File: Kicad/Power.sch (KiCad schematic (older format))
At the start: 1 part

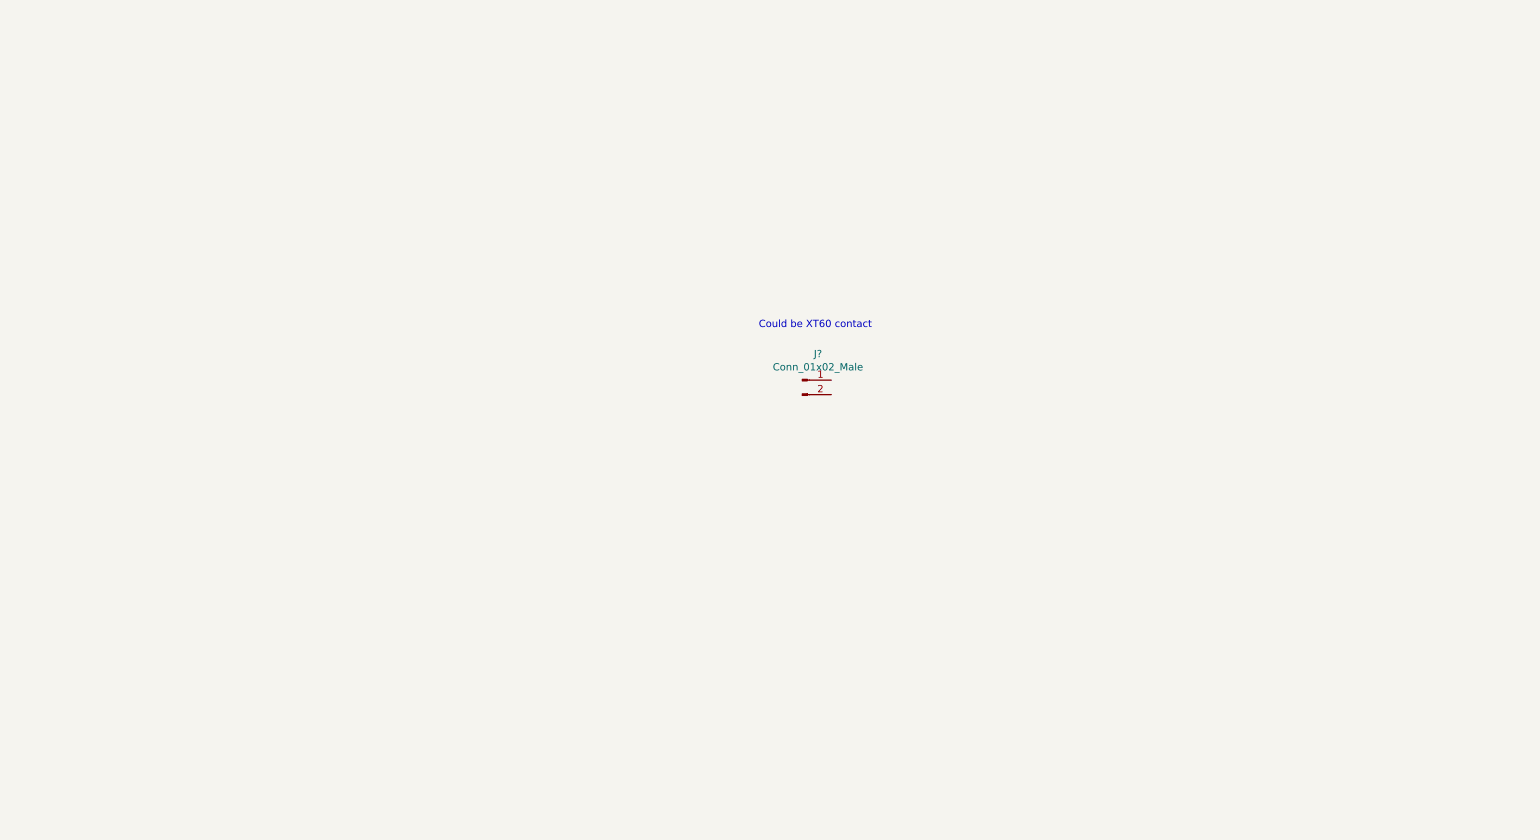
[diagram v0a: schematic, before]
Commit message: Added stepper driver and componets and power management
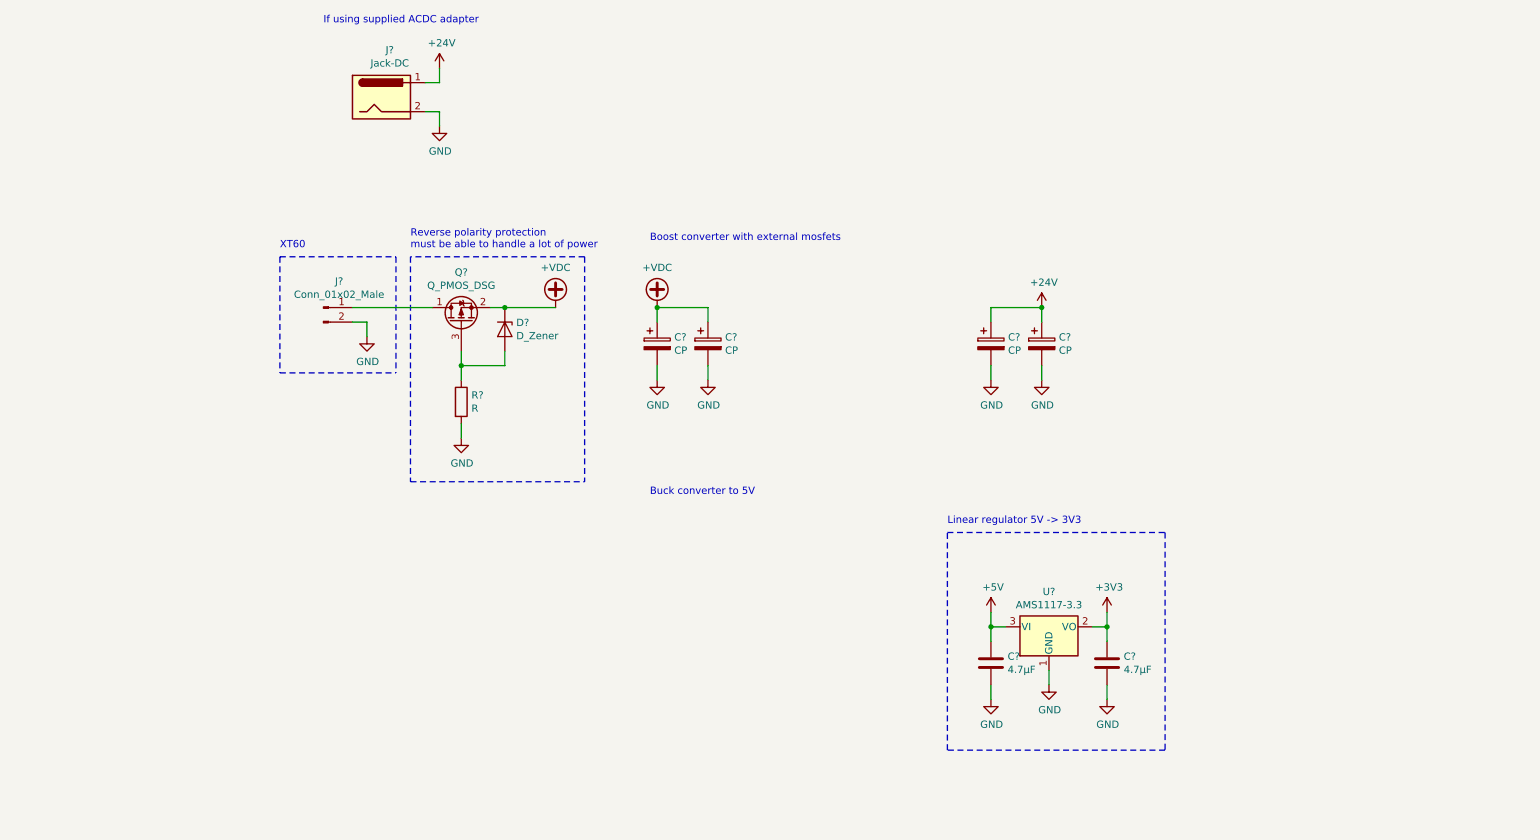
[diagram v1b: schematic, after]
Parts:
- added C? (x4): CP, symbol Device:CP
- added C? (x2): 4.7µF, symbol Device:C
- added D?: D_Zener, symbol Device:D_Zener
- added J?: Jack-DC, symbol Connector:Jack-DC
- added Q?: Q_PMOS_DSG, symbol Device:Q_PMOS_DSG
- added R?: R, symbol Device:R
- added U?: AMS1117-3.3, Package_TO_SOT_SMD:SOT-223-3_TabPin2, symbol Regulator_Linear:AMS1117-3.3
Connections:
- net at J?.1 (Pin_1): now also Q?.1 (D)
- net GND: now reaches J?.2 (Pin_2)
- net GND: now also C?.2, C?.2, C?.2, C?.2, C?.2, C?.2, J?.2, R?.2, U?.1 (GND)
- new net: D?.2 (A), Q?.3 (G), R?.1
- new net +24V: C?.1, C?.1, J?.1
- new net +3V3: C?.1, U?.2 (VO)
- new net +5V: C?.1, U?.3 (VI)
- new net +VDC: C?.1, C?.1, D?.1 (K), Q?.2 (S)
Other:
- note added: "Boost converter with external mosfets"
- note added: "Buck converter to 5V"
- note added: "If using supplied ACDC adapter"
- note added: "Linear regulator 5V -> 3V3"
- note added: "Reverse polarity protection\nmust be able to handle a lot of power"
- note added: "XT60"
- note removed: "Could be XT60 contact"
- moved on the sheet: J?

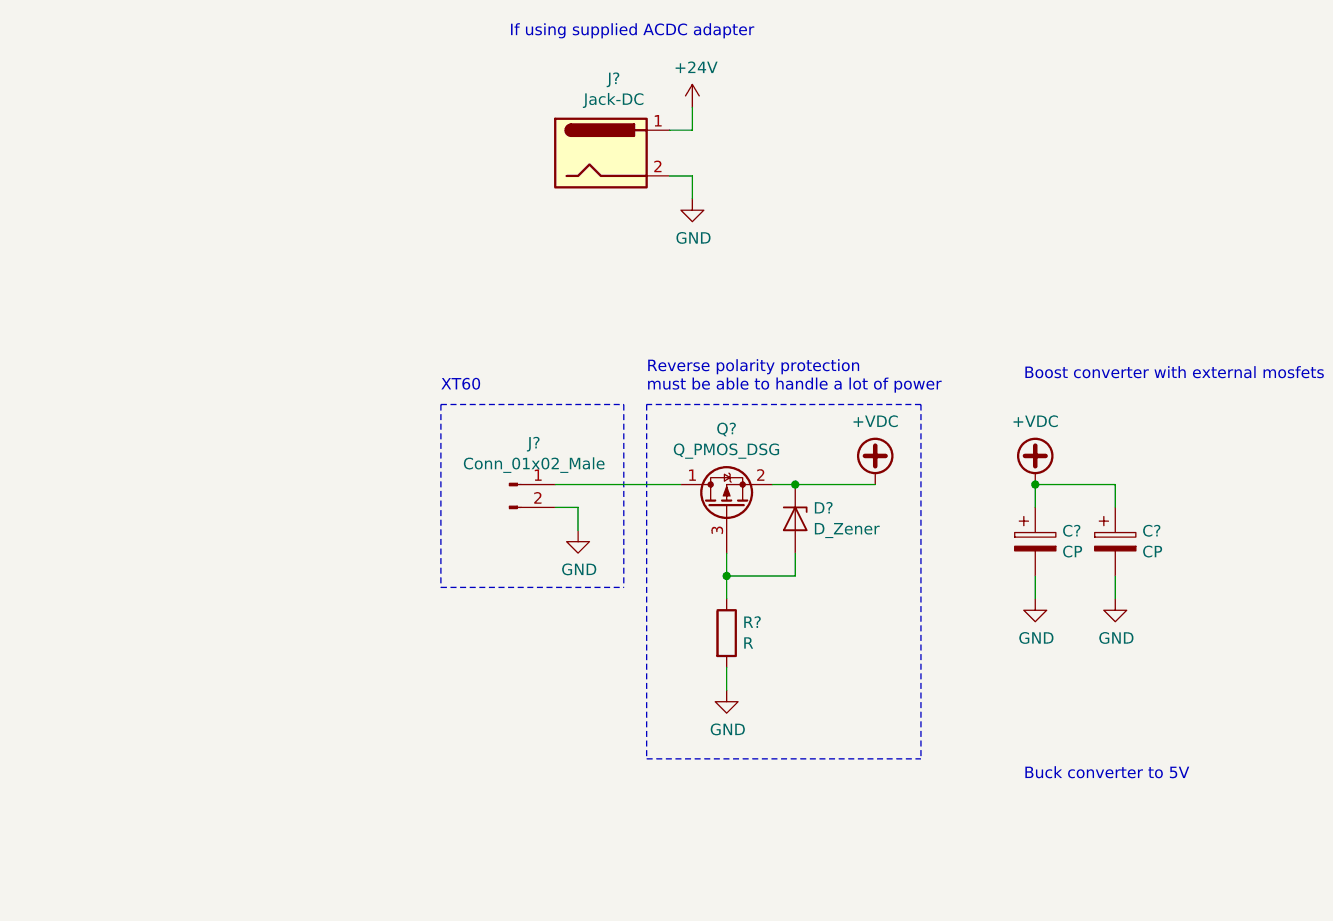
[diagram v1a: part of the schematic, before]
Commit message: Added spindle sheet
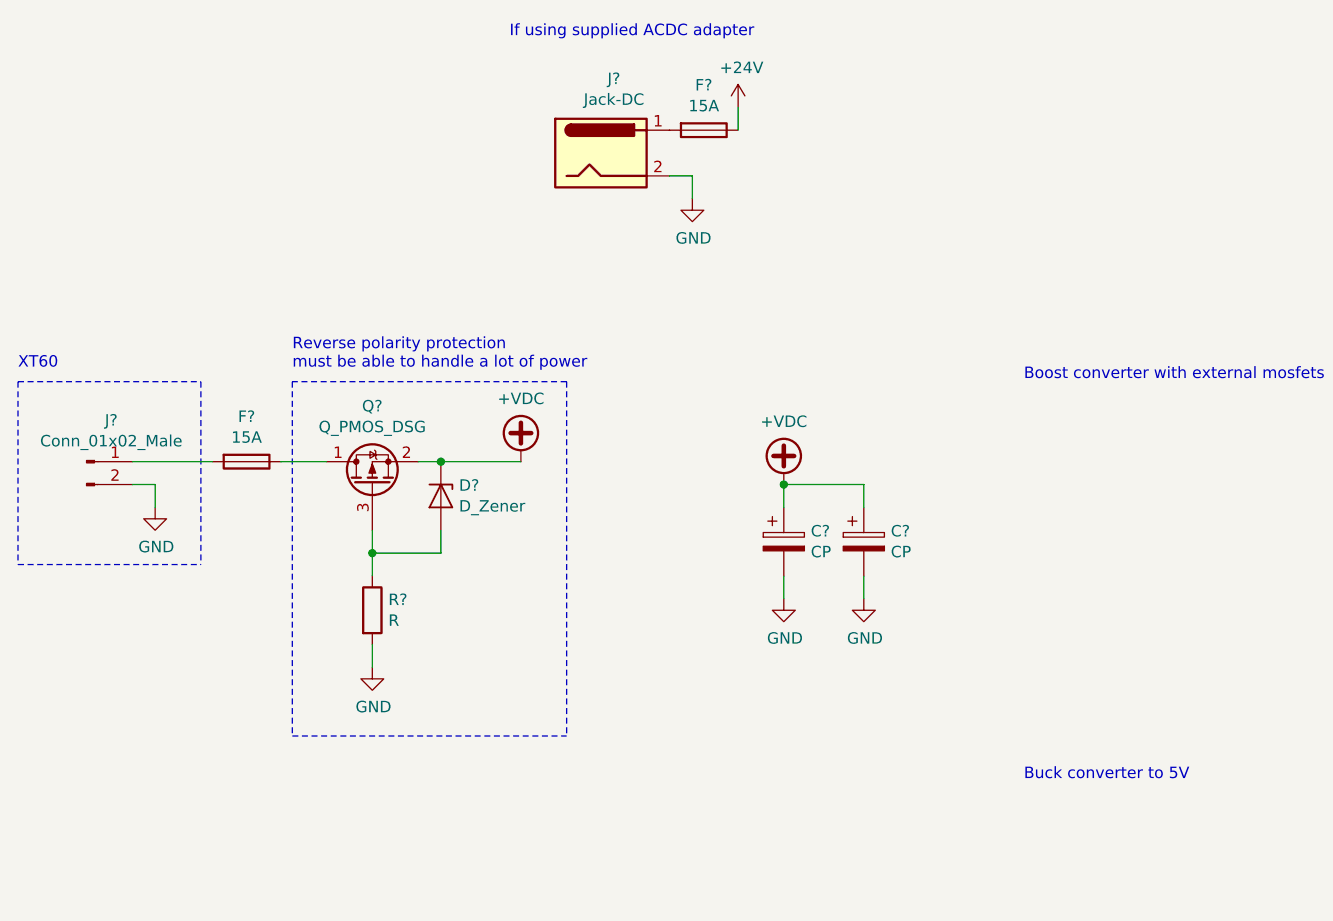
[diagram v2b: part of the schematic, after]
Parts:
- added F? (x2): 15A, symbol Device:Fuse
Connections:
- net +24V: now also F?.1; no longer J?.1
- net at J?.1 (Pin_1): now also F?.2; no longer Q?.1 (D)
- new net: F?.2, J?.1
- new net: F?.1, Q?.1 (D)
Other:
- moved on the sheet: C?, D?, J?, Q?, R?
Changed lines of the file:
@@
 $Descr A4 11693 8268
 encoding utf-8
-Sheet 3 4
+Sheet 3 5
 Title ""
 Date ""
@@
 L Connector:Conn_01x02_Male J?
 U 1 1 5E1C9929
-P 2700 3450
-F 0 "J?" H 2808 3631 50  0000 C CNN
-F 1 "Conn_01x02_Male" H 2808 3540 50  0000 C CNN
-F 2 "" H 2700 3450 50  0001 C CNN
-F 3 "~" H 2700 3450 50  0001 C CNN
-	1    2700 3450
-	1    0    0    -1
-$EndComp
-Text Notes 2400 3050 0    50   ~ 0
+P 850 3350
+F 0 "J?" H 958 3531 50  0000 C CNN
+F 1 "Conn_01x02_Male" H 958 3440 50  0000 C CNN
+F 2 "" H 850 3350 50  0001 C CNN
+F 3 "~" H 850 3350 50  0001 C CNN
+	1    850  3350
+	1    0    0    -1
+$EndComp
+Text Notes 550  2950 0    50   ~ 0
 XT60
 Text Notes 4950 3000 0    50   ~ 0
@@
 L power:+VDC #PWR0110
 U 1 1 5E1F3FCE
-P 4300 3450
-F 0 "#PWR0110" H 4300 3350 50  0001 C CNN
-F 1 "+VDC" H 4300 3725 50  0000 C CNN
-F 2 "" H 4300 3450 50  0001 C CNN
-F 3 "" H 4300 3450 50  0001 C CNN
-	1    4300 3450
+P 2750 3350
+F 0 "#PWR0110" H 2750 3250 50  0001 C CNN
+F 1 "+VDC" H 2750 3625 50  0000 C CNN
+F 2 "" H 2750 3350 50  0001 C CNN
+F 3 "" H 2750 3350 50  0001 C CNN
+	1    2750 3350
 	1    0    0    -1
 $EndComp
@@
 L power:GND #PWR0111
 U 1 1 5E1F4248
-P 3000 3650
-F 0 "#PWR0111" H 3000 3400 50  0001 C CNN
-F 1 "GND" H 3005 3477 50  0000 C CNN
-F 2 "" H 3000 3650 50  0001 C CNN
-F 3 "" H 3000 3650 50  0001 C CNN
-	1    3000 3650
+P 1150 3550
+F 0 "#PWR0111" H 1150 3300 50  0001 C CNN
+F 1 "GND" H 1155 3377 50  0000 C CNN
+F 2 "" H 1150 3550 50  0001 C CNN
+F 3 "" H 1150 3550 50  0001 C CNN
+	1    1150 3550
 	1    0    0    -1
 $EndComp
@@
 L power:+24V #PWR0113
 U 1 1 5E1F962C
-P 3500 1800
-F 0 "#PWR0113" H 3500 1650 50  0001 C CNN
-F 1 "+24V" H 3515 1973 50  0000 C CNN
-F 2 "" H 3500 1800 50  0001 C CNN
-F 3 "" H 3500 1800 50  0001 C CNN
-	1    3500 1800
-	1    0    0    -1
-$EndComp
-Wire Wire Line
-	3500 1800 3500 1900
-Wire Wire Line
-	3500 1900 3400 1900
+P 3700 1800
+F 0 "#PWR0113" H 3700 1650 50  0001 C CNN
+F 1 "+24V" H 3715 1973 50  0000 C CNN
+F 2 "" H 3700 1800 50  0001 C CNN
+F 3 "" H 3700 1800 50  0001 C CNN
+	1    3700 1800
+	1    0    0    -1
+$EndComp
 Wire Wire Line
 	3400 2100 3500 2100
@@
 L Device:Q_PMOS_DSG Q?
 U 1 1 5E1FCACA
-P 3650 3550
-F 0 "Q?" V 3993 3550 50  0000 C CNN
-F 1 "Q_PMOS_DSG" V 3902 3550 50  0000 C CNN
-F 2 "" H 3850 3650 50  0001 C CNN
-F 3 "~" H 3650 3550 50  0001 C CNN
-	1    3650 3550
+P 2100 3450
+F 0 "Q?" V 2443 3450 50  0000 C CNN
+F 1 "Q_PMOS_DSG" V 2352 3450 50  0000 C CNN
+F 2 "" H 2300 3550 50  0001 C CNN
+F 3 "~" H 2100 3450 50  0001 C CNN
+	1    2100 3450
 	0    -1   -1   0
 $EndComp
@@
 L power:GND #PWR0114
 U 1 1 5E20125D
-P 3650 4350
-F 0 "#PWR0114" H 3650 4100 50  0001 C CNN
-F 1 "GND" H 3655 4177 50  0000 C CNN
-F 2 "" H 3650 4350 50  0001 C CNN
-F 3 "" H 3650 4350 50  0001 C CNN
-	1    3650 4350
-	1    0    0    -1
-$EndComp
-Wire Wire Line
-	3950 3850 3650 3850
-Wire Wire Line
-	3950 3750 3950 3850
-Wire Wire Line
-	3650 3750 3650 3850
+P 2100 4250
+F 0 "#PWR0114" H 2100 4000 50  0001 C CNN
+F 1 "GND" H 2105 4077 50  0000 C CNN
+F 2 "" H 2100 4250 50  0001 C CNN
+F 3 "" H 2100 4250 50  0001 C CNN
+	1    2100 4250
+	1    0    0    -1
+$EndComp
+Wire Wire Line
+	2400 3750 2100 3750
+Wire Wire Line
+	2400 3650 2400 3750
+Wire Wire Line
+	2100 3650 2100 3750
 $Comp
 L Device:R R?
 U 1 1 5E202E4D
-P 3650 4100
-F 0 "R?" H 3720 4146 50  0000 L CNN
-F 1 "R" H 3720 4055 50  0000 L CNN
-F 2 "" V 3580 4100 50  0001 C CNN
-F 3 "~" H 3650 4100 50  0001 C CNN
-	1    3650 4100
-	1    0    0    -1
-$EndComp
-Wire Wire Line
-	3650 3850 3650 3950
-Connection ~ 3650 3850
-Wire Wire Line
-	3650 4250 3650 4350
-Wire Wire Line
-	3000 3650 3000 3550
-Wire Wire Line
-	3000 3550 2900 3550
-Wire Notes Line
-	4500 3100 3300 3100
-Wire Notes Line
-	3300 4650 4500 4650
-Text Notes 3300 3050 0    50   ~ 0
+P 2100 4000
+F 0 "R?" H 2170 4046 50  0000 L CNN
+F 1 "R" H 2170 3955 50  0000 L CNN
+F 2 "" V 2030 4000 50  0001 C CNN
+F 3 "~" H 2100 4000 50  0001 C CNN
+	1    2100 4000
+	1    0    0    -1
+$EndComp
+Wire Wire Line
+	2100 3750 2100 3850
+Connection ~ 2100 3750
+Wire Wire Line
+	2100 4150 2100 4250
+Wire Wire Line
+	1150 3550 1150 3450
+Wire Wire Line
+	1150 3450 1050 3450
+Wire Notes Line
+	2950 3000 1750 3000
+Wire Notes Line
+	1750 4550 2950 4550
+Text Notes 1750 2950 0    50   ~ 0
 Reverse polarity protection\nmust be able to handle a lot of power
-Wire Wire Line
-	2900 3450 3450 3450
-Wire Notes Line
-	2400 3100 3200 3100
-Wire Notes Line
-	2400 3900 3200 3900
-Wire Notes Line
-	2400 3100 2400 3900
-Wire Notes Line
-	3200 3100 3200 3900
-Wire Notes Line
-	3300 3100 3300 4650
-Wire Notes Line
-	4500 3100 4500 4650
+Wire Notes Line
+	550  3000 1350 3000
+Wire Notes Line
+	550  3800 1350 3800
+Wire Notes Line
+	550  3000 550  3800
+Wire Notes Line
+	1350 3000 1350 3800
+Wire Notes Line
+	1750 3000 1750 4550
+Wire Notes Line
+	2950 3000 2950 4550
 $Comp
 L Device:CP C?
 U 1 1 5E20A92D
-P 5000 3700
-F 0 "C?" H 5118 3746 50  0000 L CNN
-F 1 "CP" H 5118 3655 50  0000 L CNN
-F 2 "" H 5038 3550 50  0001 C CNN
-F 3 "~" H 5000 3700 50  0001 C CNN
-	1    5000 3700
+P 3900 3700
+F 0 "C?" H 4018 3746 50  0000 L CNN
+F 1 "CP" H 4018 3655 50  0000 L CNN
+F 2 "" H 3938 3550 50  0001 C CNN
+F 3 "~" H 3900 3700 50  0001 C CNN
+	1    3900 3700
 	1    0    0    -1
 $EndComp
@@
 L Device:CP C?
 U 1 1 5E20B915
-P 5350 3700
-F 0 "C?" H 5468 3746 50  0000 L CNN
-F 1 "CP" H 5468 3655 50  0000 L CNN
-F 2 "" H 5388 3550 50  0001 C CNN
-F 3 "~" H 5350 3700 50  0001 C CNN
-	1    5350 3700
+P 4250 3700
+F 0 "C?" H 4368 3746 50  0000 L CNN
+F 1 "CP" H 4368 3655 50  0000 L CNN
+F 2 "" H 4288 3550 50  0001 C CNN
+F 3 "~" H 4250 3700 50  0001 C CNN
+	1    4250 3700
 	1    0    0    -1
 $EndComp
@@
 L power:GND #PWR0115
 U 1 1 5E20BAD0
-P 5000 3950
-F 0 "#PWR0115" H 5000 3700 50  0001 C CNN
-F 1 "GND" H 5005 3777 50  0000 C CNN
-F 2 "" H 5000 3950 50  0001 C CNN
-F 3 "" H 5000 3950 50  0001 C CNN
-	1    5000 3950
+P 3900 3950
+F 0 "#PWR0115" H 3900 3700 50  0001 C CNN
+F 1 "GND" H 3905 3777 50  0000 C CNN
+F 2 "" H 3900 3950 50  0001 C CNN
+F 3 "" H 3900 3950 50  0001 C CNN
+	1    3900 3950
 	1    0    0    -1
 $EndComp
@@
 L power:GND #PWR0116
 U 1 1 5E20BDE3
-P 5350 3950
-F 0 "#PWR0116" H 5350 3700 50  0001 C CNN
-F 1 "GND" H 5355 3777 50  0000 C CNN
-F 2 "" H 5350 3950 50  0001 C CNN
-F 3 "" H 5350 3950 50  0001 C CNN
-	1    5350 3950
-	1    0    0    -1
-$EndComp
-Wire Wire Line
-	5000 3850 5000 3950
-Wire Wire Line
-	5350 3850 5350 3950
-Wire Wire Line
-	5350 3550 5350 3450
-Wire Wire Line
-	5350 3450 5000 3450
-Wire Wire Line
-	5000 3450 5000 3550
+P 4250 3950
+F 0 "#PWR0116" H 4250 3700 50  0001 C CNN
+F 1 "GND" H 4255 3777 50  0000 C CNN
+F 2 "" H 4250 3950 50  0001 C CNN
+F 3 "" H 4250 3950 50  0001 C CNN
+	1    4250 3950
+	1    0    0    -1
+$EndComp
+Wire Wire Line
+	3900 3850 3900 3950
+Wire Wire Line
+	4250 3850 4250 3950
+Wire Wire Line
+	4250 3550 4250 3450
+Wire Wire Line
+	4250 3450 3900 3450
+Wire Wire Line
+	3900 3450 3900 3550
 $Comp
 L power:+VDC #PWR0117
 U 1 1 5E20CAD1
-P 5000 3450
-F 0 "#PWR0117" H 5000 3350 50  0001 C CNN
-F 1 "+VDC" H 5000 3725 50  0000 C CNN
-F 2 "" H 5000 3450 50  0001 C CNN
-F 3 "" H 5000 3450 50  0001 C CNN
-	1    5000 3450
-	1    0    0    -1
-$EndComp
-Connection ~ 5000 3450
-Wire Wire Line
-	3850 3450 3950 3450
+P 3900 3450
+F 0 "#PWR0117" H 3900 3350 50  0001 C CNN
+F 1 "+VDC" H 3900 3725 50  0000 C CNN
+F 2 "" H 3900 3450 50  0001 C CNN
+F 3 "" H 3900 3450 50  0001 C CNN
+	1    3900 3450
+	1    0    0    -1
+$EndComp
+Connection ~ 3900 3450
+Wire Wire Line
+	2300 3350 2400 3350
 $Comp
 L Device:D_Zener D?
 U 1 1 5E20D2EC
-P 3950 3600
-F 0 "D?" V 3904 3679 50  0000 L CNN
-F 1 "D_Zener" V 3995 3679 50  0000 L CNN
-F 2 "" H 3950 3600 50  0001 C CNN
-F 3 "~" H 3950 3600 50  0001 C CNN
-	1    3950 3600
+P 2400 3500
+F 0 "D?" V 2354 3579 50  0000 L CNN
+F 1 "D_Zener" V 2445 3579 50  0000 L CNN
+F 2 "" H 2400 3500 50  0001 C CNN
+F 3 "~" H 2400 3500 50  0001 C CNN
+	1    2400 3500
 	0    1    1    0
 $EndComp
-Connection ~ 3950 3450
-Wire Wire Line
-	3950 3450 4300 3450
+Connection ~ 2400 3350
+Wire Wire Line
+	2400 3350 2750 3350
 $Comp
 L Device:CP C?
@@
 Wire Notes Line
 	8500 6500 7000 6500
+$Comp
+L Device:Fuse F?
+U 1 1 5E27ADBA
+P 1550 3350
+F 0 "F?" V 1353 3350 50  0000 C CNN
+F 1 "15A" V 1444 3350 50  0000 C CNN
+F 2 "" V 1480 3350 50  0001 C CNN
+F 3 "~" H 1550 3350 50  0001 C CNN
+	1    1550 3350
+	0    1    1    0
+$EndComp
+Wire Wire Line
+	1900 3350 1700 3350
+Wire Wire Line
+	1400 3350 1050 3350
+Wire Wire Line
+	3700 1800 3700 1900
+$Comp
+L Device:Fuse F?
+U 1 1 5E27F7CC
+P 3550 1900
+F 0 "F?" V 3353 1900 50  0000 C CNN
+F 1 "15A" V 3444 1900 50  0000 C CNN
+F 2 "" V 3480 1900 50  0001 C CNN
+F 3 "~" H 3550 1900 50  0001 C CNN
+	1    3550 1900
+	0    1    1    0
+$EndComp
 $EndSCHEMATC

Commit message: Added TMC2130 to board and routed
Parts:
- added C10: 4.7µF, symbol Device:C
- added C11, C12, C9: F, symbol Device:C
- added D2: D_Schottky, PrivateLib:DPAK, symbol Device:D_Schottky
- added L1: 2.2µF, symbol Device:L
- added Q2: Q_NMOS_DSG, symbol Device:Q_NMOS_DSG
- added R2, R3, R5, R7, R8: R, symbol Device:R
- added R4: 10k, symbol Device:R
- added R6: 0.01R, symbol Device:R
- added U2: LM5155, Package_SON:WSON-12-1EP_3x2mm_P0.5mm_EP1x2.65_ThermalVias, symbol PrivateLib:LM5155
- F1: renamed from F?; footprint (none) -> Fuse:Fuse_2512_6332Metric
- J1: renamed from J?; footprint (none) -> PrivateLib:XT60PW-F
- Q1: renamed from Q?; footprint (none) -> Package_TO_SOT_SMD:TO-252-2
- gave numbers to parts that had none: 11
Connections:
- net +24V: now also C12.1, D2.1 (K), R7.1
- net +VDC: now also L1.1, R2.1, U2.1 (BIAS)
- net GND: now also J1.1 (Pin_1), C10.2, C9.2, R3.2, R4.1, R6.2, R8.2, U2.13 (EP), U2.4 (PGND); no longer J1.2 (Pin_2)
- net at F1.2: now also J1.2 (Pin_2); no longer J1.1 (Pin_1)
- new net: R4.2, U2.10 (RT)
- new net: R2.2, R3.1, U2.12 (UVLO/SYNC)
- new net: C10.1, U2.2 (VCC)
- new net: Q2.3 (G), U2.3 (GATE)
- new net: Q2.2 (S), R6.1, U2.5 (CS)
- new net: R5.1, U2.6 (COMP)
- new net: C12.2, R7.2, R8.1, U2.8 (FB)
- new net: C9.1, U2.9 (SS)
- new net: D2.2 (A), L1.2, Q2.1 (D)
- new net: C11.1, R5.2
- new net GNDA: C11.2, U2.7 (AGND)
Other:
- moved on the sheet: C15, C16, J1, U3
